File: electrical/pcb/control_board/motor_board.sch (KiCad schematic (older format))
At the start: 101 parts, among them J1 ED2627-ND, J11 S7038-ND, J12 PEC10DAAN, J13 ED1501-ND, J14 ED2989-ND-USB, J15 ED2580-ND, J16 ED2580-ND, J17 ED2744-ND, J18 ED2744-ND, J19 ED2744-ND, J2 ED2627-ND, J20 ED2744-ND, J21 ED2744-ND, J22 ED2744-ND, J23 ED2744-ND, J24 ED2744-ND, J25 ED2744-ND, J26 ED2744-ND, J28 ED2580-ND, J29 ED2580-ND, J3 ED2627-ND, J30 ED2580-ND, J31 ED2580-ND, J33 ina260_Vin, J34 ina260_8pin, J4 ED2627-ND, J5 ED2627-ND, J9 S7038-ND, M1 Mounting_Holes, T1 test_point, T10 test_point, T11 test_point, T12 test_point, T13 test_point, T14 test_point, T15 test_point, T16 test_point, T17 test_point, T18 test_point, T19 test_point, T2 test_point, T20 test_point, T21 test_point, T3 test_point, T4 test_point, T5 test_point, T6 test_point, T7 test_point, T8 test_point, T9 test_point, U1 LM358-N, U2 LM358-N, y1 rover_silkscreen

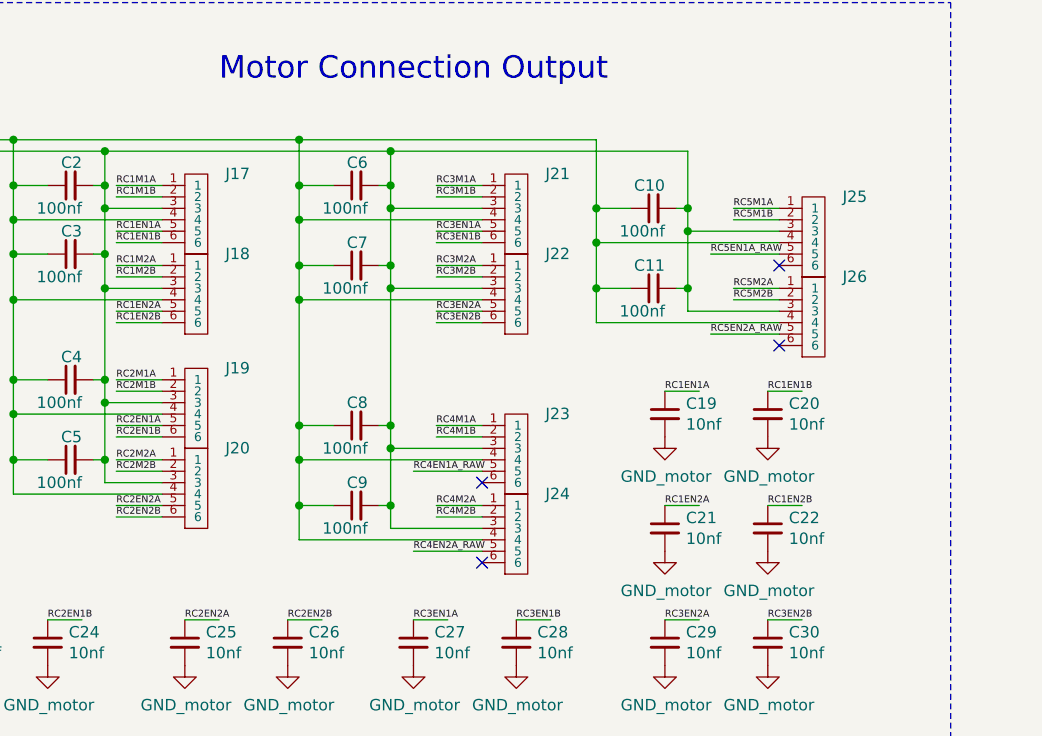
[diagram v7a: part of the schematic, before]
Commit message: Adding molex connectors for motor output
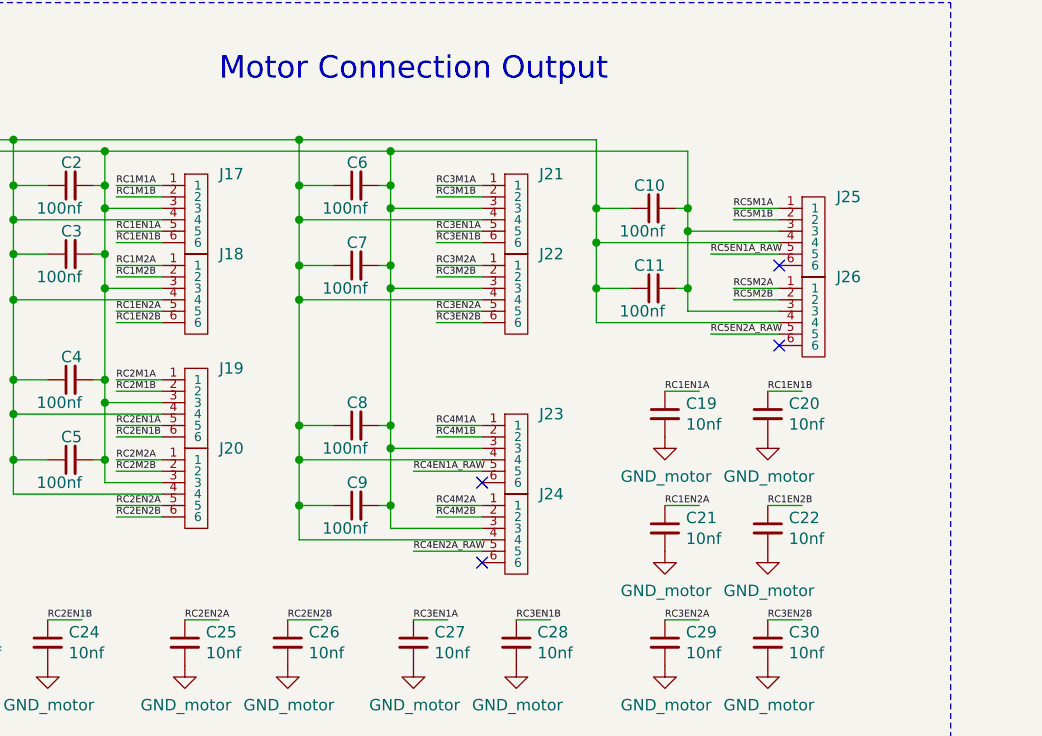
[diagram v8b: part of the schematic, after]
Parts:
- removed J17, J18, J19, J20, J21, J22, J23, J24, J25, J26: ED2744-ND, JPL Robotics:ED2744-ND, symbol JPL_Robotics_Lib:ED2744-ND
- added J17, J18, J19, J20, J21, J22, J23, J24, J25, J26: Molex_172675-0613, symbol JPL_Robotics_Lib:Molex_172675-0613
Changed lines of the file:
@@
 NoConn ~ 5000 3450
-$Comp
-L JPL_Robotics_Lib:ED2744-ND J?
-U 1 1 60B1CB08
-P 11500 2250
-AR Path="/60B1CB08" Ref="J?"  Part="1"
-AR Path="/60A51BAC/60B1CB08" Ref="J17"  Part="1"
-F 0 "J17" H 11477 2601 50  0000 L CNN
-F 1 "ED2744-ND" H 11477 2510 50  0001 L CNN
-F 2 "JPL Robotics:ED2744-ND" H 11300 2900 50  0001 C CNN
-F 3 "" H 11300 2900 50  0001 C CNN
-	1    11500 2250
-	1    0    0    -1
-$EndComp
 $Comp
 L JPL_Robotics_Lib:ED2627-ND J?
@@
 Text Label 11000 2200 0    30   ~ 0
 RC1EN1B
-$Comp
-L JPL_Robotics_Lib:ED2744-ND J?
-U 1 1 60B1CB26
-P 11500 2600
-AR Path="/60B1CB26" Ref="J?"  Part="1"
-AR Path="/60A51BAC/60B1CB26" Ref="J18"  Part="1"
-F 0 "J18" H 11477 2951 50  0000 L CNN
-F 1 "ED2744-ND" H 11477 2860 50  0001 L CNN
-F 2 "JPL Robotics:ED2744-ND" H 11300 3250 50  0001 C CNN
-F 3 "" H 11300 3250 50  0001 C CNN
-	1    11500 2600
-	1    0    0    -1
-$EndComp
 Text Label 11000 2300 0    30   ~ 0
 RC1M2A
@@
 Wire Wire Line
 	11000 2550 11200 2550
-$Comp
-L JPL_Robotics_Lib:ED2744-ND J?
-U 1 1 60B1CB53
-P 11500 3100
-AR Path="/60B1CB53" Ref="J?"  Part="1"
-AR Path="/60A51BAC/60B1CB53" Ref="J19"  Part="1"
-F 0 "J19" H 11477 3451 50  0000 L CNN
-F 1 "ED2744-ND" H 11477 3360 50  0001 L CNN
-F 2 "JPL Robotics:ED2744-ND" H 11300 3750 50  0001 C CNN
-F 3 "" H 11300 3750 50  0001 C CNN
-	1    11500 3100
-	1    0    0    -1
-$EndComp
 Text Label 11000 2800 0    30   ~ 0
 RC2M1A
@@
 Text Label 11000 3050 0    30   ~ 0
 RC2EN1B
-$Comp
-L JPL_Robotics_Lib:ED2744-ND J?
-U 1 1 60B1CB5D
-P 11500 3450
-AR Path="/60B1CB5D" Ref="J?"  Part="1"
-AR Path="/60A51BAC/60B1CB5D" Ref="J20"  Part="1"
-F 0 "J20" H 11477 3801 50  0000 L CNN
-F 1 "ED2744-ND" H 11477 3710 50  0001 L CNN
-F 2 "JPL Robotics:ED2744-ND" H 11300 4100 50  0001 C CNN
-F 3 "" H 11300 4100 50  0001 C CNN
-	1    11500 3450
-	1    0    0    -1
-$EndComp
 Text Label 11000 3150 0    30   ~ 0
 RC2M2A
@@
 Wire Wire Line
 	11000 3400 11200 3400
-$Comp
-L JPL_Robotics_Lib:ED2744-ND J?
-U 1 1 60B1CB6F
-P 12900 2250
-AR Path="/60B1CB6F" Ref="J?"  Part="1"
-AR Path="/60A51BAC/60B1CB6F" Ref="J21"  Part="1"
-F 0 "J21" H 12877 2601 50  0000 L CNN
-F 1 "ED2744-ND" H 12877 2510 50  0001 L CNN
-F 2 "JPL Robotics:ED2744-ND" H 12700 2900 50  0001 C CNN
-F 3 "" H 12700 2900 50  0001 C CNN
-	1    12900 2250
-	1    0    0    -1
-$EndComp
 Text Label 12400 1950 0    30   ~ 0
 RC3M1A
@@
 Text Label 12400 2200 0    30   ~ 0
 RC3EN1B
-$Comp
-L JPL_Robotics_Lib:ED2744-ND J?
-U 1 1 60B1CB79
-P 12900 2600
-AR Path="/60B1CB79" Ref="J?"  Part="1"
-AR Path="/60A51BAC/60B1CB79" Ref="J22"  Part="1"
-F 0 "J22" H 12877 2951 50  0000 L CNN
-F 1 "ED2744-ND" H 12877 2860 50  0001 L CNN
-F 2 "JPL Robotics:ED2744-ND" H 12700 3250 50  0001 C CNN
-F 3 "" H 12700 3250 50  0001 C CNN
-	1    12900 2600
-	1    0    0    -1
-$EndComp
 Text Label 12400 2300 0    30   ~ 0
 RC3M2A
@@
 Wire Wire Line
 	12400 2550 12600 2550
-$Comp
-L JPL_Robotics_Lib:ED2744-ND J?
-U 1 1 60B1CB8B
-P 12900 3300
-AR Path="/60B1CB8B" Ref="J?"  Part="1"
-AR Path="/60A51BAC/60B1CB8B" Ref="J23"  Part="1"
-F 0 "J23" H 12877 3651 50  0000 L CNN
-F 1 "ED2744-ND" H 12877 3560 50  0001 L CNN
-F 2 "JPL Robotics:ED2744-ND" H 12700 3950 50  0001 C CNN
-F 3 "" H 12700 3950 50  0001 C CNN
-	1    12900 3300
-	1    0    0    -1
-$EndComp
 Text Label 12400 3000 0    30   ~ 0
 RC4M1A
@@
 Text Label 12300 3200 0    30   ~ 0
 RC4EN1A_RAW
-$Comp
-L JPL_Robotics_Lib:ED2744-ND J?
-U 1 1 60B1CB94
-P 12900 3650
-AR Path="/60B1CB94" Ref="J?"  Part="1"
-AR Path="/60A51BAC/60B1CB94" Ref="J24"  Part="1"
-F 0 "J24" H 12877 4001 50  0000 L CNN
-F 1 "ED2744-ND" H 12877 3910 50  0001 L CNN
-F 2 "JPL Robotics:ED2744-ND" H 12700 4300 50  0001 C CNN
-F 3 "" H 12700 4300 50  0001 C CNN
-	1    12900 3650
-	1    0    0    -1
-$EndComp
 Text Label 12400 3350 0    30   ~ 0
 RC4M2A
@@
 Wire Wire Line
 	12400 3400 12600 3400
-$Comp
-L JPL_Robotics_Lib:ED2744-ND J?
-U 1 1 60B1CBA1
-P 14200 2350
-AR Path="/60B1CBA1" Ref="J?"  Part="1"
-AR Path="/60A51BAC/60B1CBA1" Ref="J25"  Part="1"
-F 0 "J25" H 14177 2701 50  0000 L CNN
-F 1 "ED2744-ND" H 14177 2610 50  0001 L CNN
-F 2 "JPL Robotics:ED2744-ND" H 14000 3000 50  0001 C CNN
-F 3 "" H 14000 3000 50  0001 C CNN
-	1    14200 2350
-	1    0    0    -1
-$EndComp
 Text Label 13700 2050 0    30   ~ 0
 RC5M1A
@@
 Text Label 13600 2250 0    30   ~ 0
 RC5EN1A_RAW
-$Comp
-L JPL_Robotics_Lib:ED2744-ND J?
-U 1 1 60B1CBAA
-P 14200 2700
-AR Path="/60B1CBAA" Ref="J?"  Part="1"
-AR Path="/60A51BAC/60B1CBAA" Ref="J26"  Part="1"
-F 0 "J26" H 14177 3051 50  0000 L CNN
-F 1 "ED2744-ND" H 14177 2960 50  0001 L CNN
-F 2 "JPL Robotics:ED2744-ND" H 14000 3350 50  0001 C CNN
-F 3 "" H 14000 3350 50  0001 C CNN
-	1    14200 2700
-	1    0    0    -1
-$EndComp
 Text Label 13700 2400 0    30   ~ 0
 RC5M2A
@@
 Text Label 3650 8900 0    50   ~ 0
 alert
+$Comp
+L JPL_Robotics_Lib:Molex_172675-0613 J17
+U 1 1 60A58E9D
+P 11300 2250
+F 0 "J17" H 11450 2600 50  0000 L CNN
+F 1 "Molex_172675-0613" H 11000 2650 50  0001 L CNN
+F 2 "" H 11350 2250 50  0001 C CNN
+F 3 "" H 11350 2250 50  0001 C CNN
+	1    11300 2250
+	1    0    0    -1
+$EndComp
+$Comp
+L JPL_Robotics_Lib:Molex_172675-0613 J18
+U 1 1 60ACADF7
+P 11300 2600
+F 0 "J18" H 11450 2950 50  0000 L CNN
+F 1 "Molex_172675-0613" H 11000 3000 50  0001 L CNN
+F 2 "" H 11350 2600 50  0001 C CNN
+F 3 "" H 11350 2600 50  0001 C CNN
+	1    11300 2600
+	1    0    0    -1
+$EndComp
+$Comp
+L JPL_Robotics_Lib:Molex_172675-0613 J19
+U 1 1 60ACBA13
+P 11300 3100
+F 0 "J19" H 11450 3450 50  0000 L CNN
+F 1 "Molex_172675-0613" H 11000 3500 50  0001 L CNN
+F 2 "" H 11350 3100 50  0001 C CNN
+F 3 "" H 11350 3100 50  0001 C CNN
+	1    11300 3100
+	1    0    0    -1
+$EndComp
+$Comp
+L JPL_Robotics_Lib:Molex_172675-0613 J20
+U 1 1 60ACC18D
+P 11300 3450
+F 0 "J20" H 11450 3800 50  0000 L CNN
+F 1 "Molex_172675-0613" H 11000 3850 50  0001 L CNN
+F 2 "" H 11350 3450 50  0001 C CNN
+F 3 "" H 11350 3450 50  0001 C CNN
+	1    11300 3450
+	1    0    0    -1
+$EndComp
+$Comp
+L JPL_Robotics_Lib:Molex_172675-0613 J21
+U 1 1 60ACDDFA
+P 12700 2250
+F 0 "J21" H 12850 2600 50  0000 L CNN
+F 1 "Molex_172675-0613" H 12400 2650 50  0001 L CNN
+F 2 "" H 12750 2250 50  0001 C CNN
+F 3 "" H 12750 2250 50  0001 C CNN
+	1    12700 2250
+	1    0    0    -1
+$EndComp
+$Comp
+L JPL_Robotics_Lib:Molex_172675-0613 J22
+U 1 1 60ACE52F
+P 12700 2600
+F 0 "J22" H 12850 2950 50  0000 L CNN
+F 1 "Molex_172675-0613" H 12400 3000 50  0001 L CNN
+F 2 "" H 12750 2600 50  0001 C CNN
+F 3 "" H 12750 2600 50  0001 C CNN
+	1    12700 2600
+	1    0    0    -1
+$EndComp
+$Comp
+L JPL_Robotics_Lib:Molex_172675-0613 J23
+U 1 1 60ACEC29
+P 12700 3300
+F 0 "J23" H 12850 3650 50  0000 L CNN
+F 1 "Molex_172675-0613" H 12400 3700 50  0001 L CNN
+F 2 "" H 12750 3300 50  0001 C CNN
+F 3 "" H 12750 3300 50  0001 C CNN
+	1    12700 3300
+	1    0    0    -1
+$EndComp
+$Comp
+L JPL_Robotics_Lib:Molex_172675-0613 J24
+U 1 1 60ACF20F
+P 12700 3650
+F 0 "J24" H 12850 4000 50  0000 L CNN
+F 1 "Molex_172675-0613" H 12400 4050 50  0001 L CNN
+F 2 "" H 12750 3650 50  0001 C CNN
+F 3 "" H 12750 3650 50  0001 C CNN
+	1    12700 3650
+	1    0    0    -1
+$EndComp
+$Comp
+L JPL_Robotics_Lib:Molex_172675-0613 J25
+U 1 1 60ACF8B7
+P 14000 2350
+F 0 "J25" H 14150 2700 50  0000 L CNN
+F 1 "Molex_172675-0613" H 13700 2750 50  0001 L CNN
+F 2 "" H 14050 2350 50  0001 C CNN
+F 3 "" H 14050 2350 50  0001 C CNN
+	1    14000 2350
+	1    0    0    -1
+$EndComp
+$Comp
+L JPL_Robotics_Lib:Molex_172675-0613 J26
+U 1 1 60AD010F
+P 14000 2700
+F 0 "J26" H 14150 3050 50  0000 L CNN
+F 1 "Molex_172675-0613" H 13700 3100 50  0001 L CNN
+F 2 "" H 14050 2700 50  0001 C CNN
+F 3 "" H 14050 2700 50  0001 C CNN
+	1    14000 2700
+	1    0    0    -1
+$EndComp
 $EndSCHEMATC
